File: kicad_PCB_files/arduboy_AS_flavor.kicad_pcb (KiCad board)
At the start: 2 copper layers, 50.6 x 82.6 mm, 119 parts, among them J1 SSD1306_SSH1106, J2 Expansion_port_NEW, J3 USB_B_Micro, Q1 2N7002, Q2 Si2301CDS, SW1 RST Button, SW2 UP Button, SW3 DOWN Button, SW4 LEFT Button, SW5 RIGHT Button, SW6 A Button, SW7 B Button, U1 ATmega32U4-MU, U1B1 ATmega32U4-AU, U2 W25Q128JVSIQ, U3 XC6206P33, U4 TP4054, U5 MPU-6050, Y1 16MHz

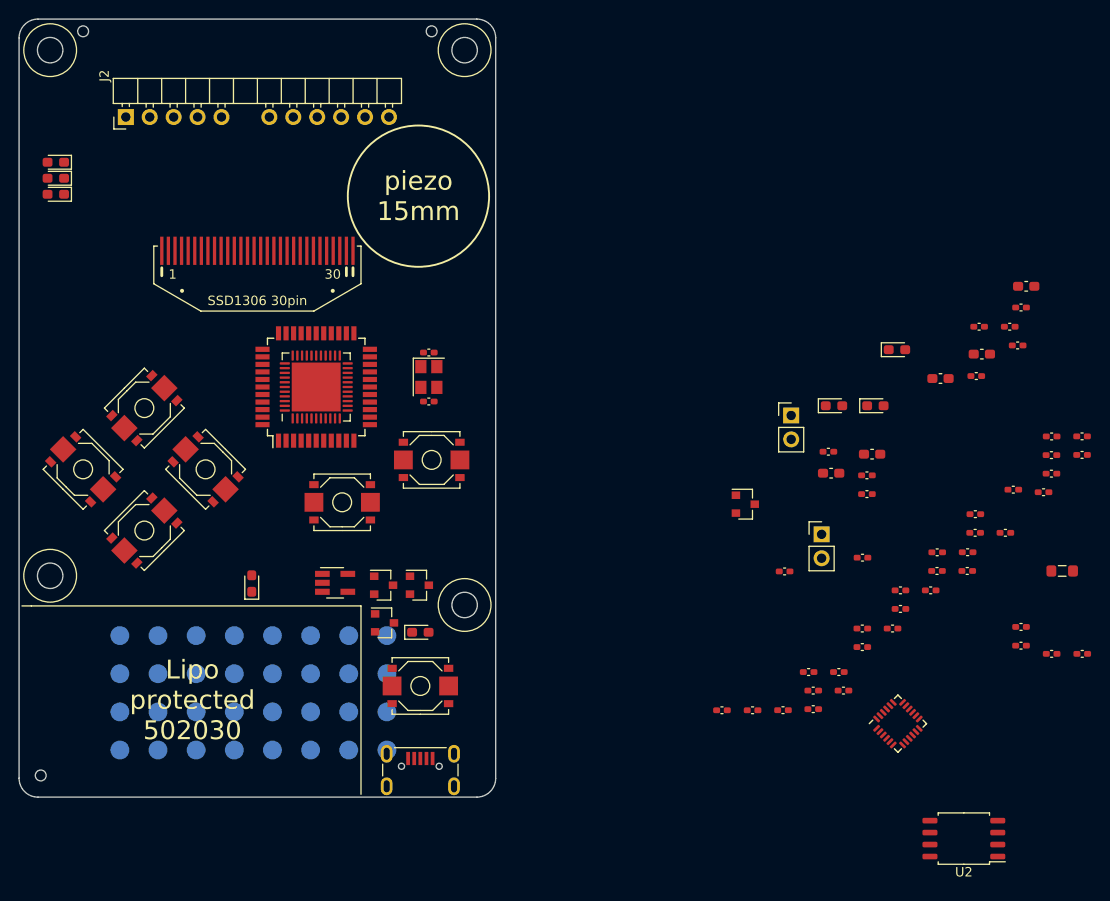
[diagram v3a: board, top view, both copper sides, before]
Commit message: Changed reset circuit Continued PCB placement feasibility Changed piezo footprint
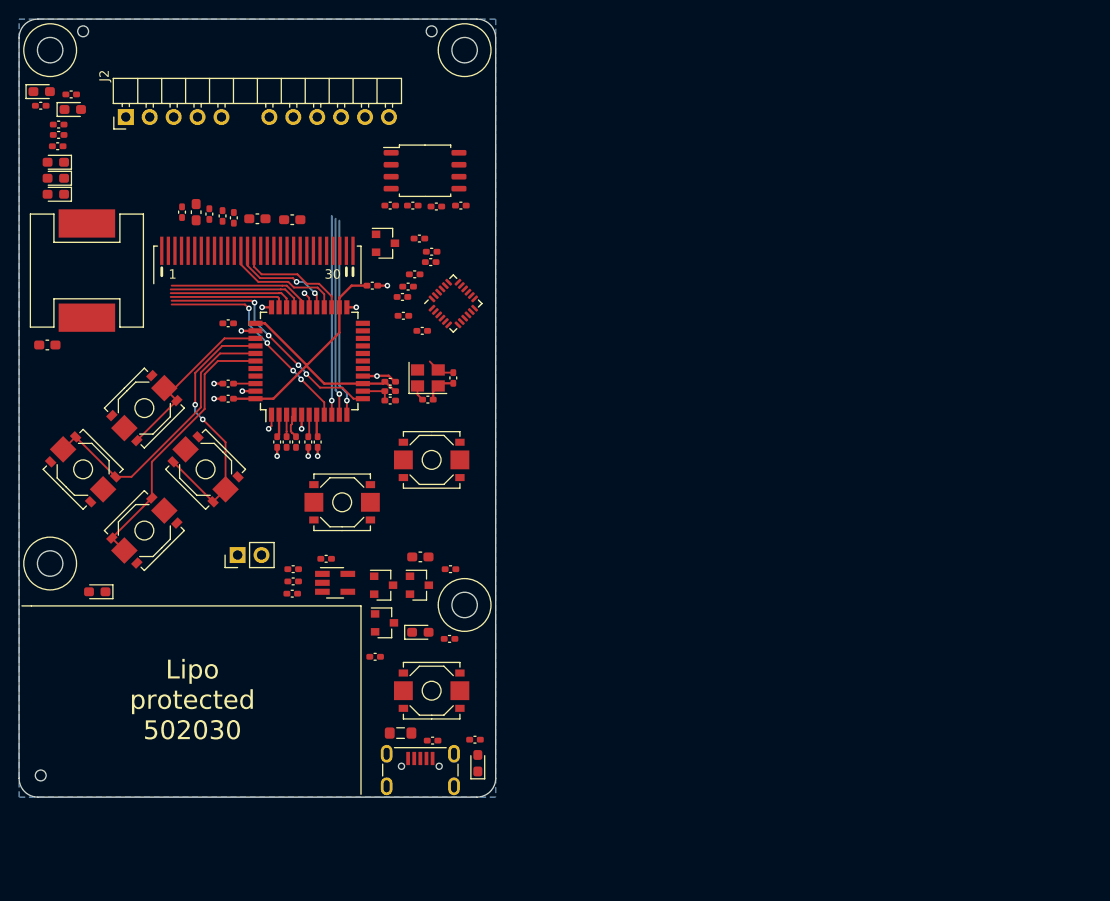
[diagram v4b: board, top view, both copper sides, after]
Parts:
- removed TP1: GYRO_INT, TestPoint:TestPoint_Pad_D2.0mm
- removed TP10: D4/D4/~OLED_DC, TestPoint:TestPoint_Pad_D2.0mm
- removed TP11: D14/PB3/MISO, TestPoint:TestPoint_Pad_D2.0mm
- removed TP12: D6/D7/~OLED_RST, TestPoint:TestPoint_Pad_D2.0mm
- removed TP13: D16/PB2/MOSI, TestPoint:TestPoint_Pad_D2.0mm
- removed TP14: D12/D6/~OLED_CS, TestPoint:TestPoint_Pad_D2.0mm
- removed TP15: D15/PB1/SCK, TestPoint:TestPoint_Pad_D2.0mm
- removed TP16: USB_ID, TestPoint:TestPoint_Pad_D2.0mm
- removed TP17: D7/E6/A, TestPoint:TestPoint_Pad_D2.0mm
- removed TP18: A4/F1/EN, TestPoint:TestPoint_Pad_D2.0mm
- removed TP19: D8/PB4/B, TestPoint:TestPoint_Pad_D2.0mm
- removed TP2: D2/PD1/SDA+FLASH_CS, TestPoint:TestPoint_Pad_D2.0mm
- removed TP20: A5/F0, TestPoint:TestPoint_Pad_D2.0mm
- removed TP21: A0/PF7/UP, TestPoint:TestPoint_Pad_D2.0mm
- removed TP22: D1/PD3/TX, TestPoint:TestPoint_Pad_D2.0mm
- removed TP23: A1/F6/RIGHT, TestPoint:TestPoint_Pad_D2.0mm
- removed TP24: D0/PD2/RX, TestPoint:TestPoint_Pad_D2.0mm
- removed TP25: A2/F5/LEFT, TestPoint:TestPoint_Pad_D2.0mm
- removed TP26: D13/PC7/SPKR2, TestPoint:TestPoint_Pad_D2.0mm
- removed TP27: A3/F4/DOWN, TestPoint:TestPoint_Pad_D2.0mm
- removed TP28: D5/PC6/SPKR1, TestPoint:TestPoint_Pad_D2.0mm
- removed TP29: 3V3, TestPoint:TestPoint_Pad_D2.0mm
- removed TP3: ~RST, TestPoint:TestPoint_Pad_D2.0mm
- removed TP30: VCC, TestPoint:TestPoint_Pad_D2.0mm
- removed TP31: 5V_USB, TestPoint:TestPoint_Pad_D2.0mm
- removed TP32: GND, TestPoint:TestPoint_Pad_D2.0mm
- removed TP4: D3/PD0/SCL, TestPoint:TestPoint_Pad_D2.0mm
- removed TP5: D11/PB7/~LED_G, TestPoint:TestPoint_Pad_D2.0mm
- removed TP6: D17/PB0/~RX_LED, TestPoint:TestPoint_Pad_D2.0mm
- removed TP7: D10/PB6/~LED_R, TestPoint:TestPoint_Pad_D2.0mm
- removed TP8: D30/D5/~TX_LED, TestPoint:TestPoint_Pad_D2.0mm
- removed TP9: D9/PB5/~LED_B, TestPoint:TestPoint_Pad_D2.0mm
- removed the U1 at (53.2, 60.8)
- JP1: footprint Connector_PinHeader_2.54mm:PinHeader_1x02_P2.54mm_Vertical -> arduboy:CPT-12123-81-SMT
- moved R13 112.9 mm to (24.0, 30.9)
- moved R10 104.5 mm to (25.9, 32.9)
- moved R15 104.1 mm to (24.7, 56.3)
- moved R14 104.0 mm to (27.2, 29.7)
- moved R11 95.7 mm to (25.9, 34.0)
- moved C5 93.8 mm to (39.0, 42.2), turned to 90 degrees
- moved R9 93.5 mm to (25.8, 35.2)
- moved C6 93.4 mm to (41.9, 42.4), turned to 90 degrees
- moved D9 91.1 mm to (27.4, 31.3)
- moved U2 91.1 mm to (64.8, 37.8), turned to 0 degrees
- moved C11 91.0 mm to (44.5, 42.8), turned to 90 degrees
- moved D8 90.5 mm to (24.1, 29.4)
- moved C13 81.9 mm to (50.7, 82.7)
- moved C10 81.7 mm to (43.3, 42.6), turned to 90 degrees
- moved R17 81.0 mm to (40.5, 42.2), turned to 90 degrees
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- renumbered U1B1 to U1
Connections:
- C17 pad 1: VBUS -> +5V
- C18 pad 1: VBUS -> +5V
- C2 pad 1: XTAL2 -> XTAL1
- C3 pad 1: XTAL1 -> XTAL2
- Y1 pad 1: XTAL1 -> XTAL2
- Y1 pad 3: XTAL2 -> XTAL1
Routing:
- net VCC: track 0.00 -> 39.4 mm
- net Btn_LEFT: track 0.00 -> 30.3 mm
- net Btn_DOWN: track 0.00 -> 29.3 mm
- net Btn_RIGHT: track 0.00 -> 29.2 mm, vias 0 -> 2
- net LED_G: track 0.00 -> 25.8 mm, vias 0 -> 4
- net RX_LED: track 0.00 -> 23.0 mm, vias 0 -> 4
- net SCK: track 0.00 -> 21.1 mm, vias 0 -> 1
- net MOSI: track 0.00 -> 21.0 mm, vias 0 -> 1
- net MISO: track 0.00 -> 20.9 mm, vias 0 -> 1
- net Btn_UP: track 0.00 -> 19.7 mm
- net GND: track 0.00 -> 19.2 mm, vias 0 -> 12
- net LED_B: track 0.00 -> 15.2 mm
- net LED_R: track 0.00 -> 14.4 mm
- net SPKR1: track 0.00 -> 13.5 mm
- net OLED_CS: track 0.00 -> 13.0 mm
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- added copper zone on B.Cu, net GND
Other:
- net class Default: trace_width 0.25 -> 0.2; via_dia 0.8 -> 0.6; via_drill 0.4 -> 0.3
- net class Power added: clearance 0.2, trace_width 0.25, via_dia 0.6, via_drill 0.3
- rule pad_to_mask_clearance: 0 -> 0.05
- rule trace_min: 0.2 -> 0.15
- board text removed: "Todo: Add dpad hole"
- board text removed: "piezo 15mm"

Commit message: Major changes, practically v2
Changed board shape
Changed a great part of the schematic
Component placement done
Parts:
- removed C23: 10nF, no_refdes:0402_HandSolder
- removed C24, C26: 100nF, no_refdes:0402_HandSolder
- removed C25: 2.2nF, no_refdes:0402_HandSolder
- removed C27: 1uF, no_refdes:0402_HandSolder
- removed D1: BAV70, Package_TO_SOT_SMD:SOT-23
- removed D5, D6: Yellow, LED_SMD:LED_0603_1608Metric_Pad1.05x0.95mm_HandSolder
- removed JP1: Speaker, arduboy:CPT-12123-81-SMT
- removed JP2: LiPo, Connector_PinHeader_2.54mm:PinHeader_1x02_P2.54mm_Vertical
- removed Q1: 2N7002, Package_TO_SOT_SMD:SOT-23
- removed Q2: Si2301CDS, Package_TO_SOT_SMD:SOT-23
- removed R15: 220, no_refdes:0603_HandSolder
- removed U5: MPU-6050, Sensor_Motion:InvenSense_QFN-24_4x4mm_P0.5mm
- added BZ1: Buzzer, arduboy:Buzzer_KLJ-5020, F.Cu at (68.0, 51.0)
- added R22: 120, no_refdes:0402_HandSolder, F.Cu at (50.9, 34.0)
- added R23: 120, no_refdes:0402_HandSolder, F.Cu at (53.3, 34.0)
- added R24: 120, no_refdes:0402_HandSolder, F.Cu at (55.9, 34.0)
- added TP1: Lipo [+], TestPoint:TestPoint_Pad_2.0x2.0mm, F.Cu at (34.8, 88.0)
- added TP16: Lipo (-), TestPoint:TestPoint_Pad_D2.0mm, F.Cu at (48.0, 80.5)
- C1: value 100nF -> 10uF; footprint no_refdes:0402_HandSolder -> no_refdes:0603_HandSolder
- C15: value 2.2uF -> 4.7uF
- C8: value 1uF -> 10uF; footprint no_refdes:0402_HandSolder -> no_refdes:0603_HandSolder
- C9: value 1uF -> 4.7uF; footprint no_refdes:0402_HandSolder -> no_refdes:0603_HandSolder
- J1: value SSD1306_SSH1106 -> SSD1306
- J2: footprint arduboy:PinHeader_1x12_P2.54mm_SLOTTED_ROTATED -> arduboy:ExpansionPort_SMD
- R12: value 6.8k -> 1.2k
- R13: value 3.3k -> 1.2k
- R14: value 3.3k -> 4.7k
- R18, R19: value 4.7k -> 120
- R5, R8: value 10k -> 120
- R6: value 6.8k -> 120
- R7: value 3.3k -> 120
- SW1: value RST Button -> ON/OFF; footprint arduboy:button_TS-1187A-B-A-B -> arduboy:Switch_DPDT_MSK12CO2-BDM
- U3: value XC6206P33 -> SRV05-4; footprint Package_TO_SOT_SMD:SOT-23 -> Package_TO_SOT_SMD:SOT-23-6
- moved H5 87.1 mm to (25.5, 100.5)
- moved R6 72.9 mm to (35.6, 34.0), turned to 180 degrees
- moved R5 61.4 mm to (33.0, 34.0), turned to 180 degrees
- moved R7 61.0 mm to (38.1, 34.0), turned to 180 degrees
- moved D7 60.4 mm to (68.5, 36.0), turned to 0 degrees
- moved U3 54.1 mm to (38.2, 94.8), turned to -90 degrees
- moved H7 54.0 mm to (25.5, 25.5)
- moved R8 53.3 mm to (40.6, 34.0), turned to 180 degrees
- moved D8 45.1 mm to (68.5, 37.5)
- moved C7 44.9 mm to (44.0, 38.8), turned to 90 degrees
- moved R12 44.3 mm to (63.0, 37.5), turned to 180 degrees
- moved H4 43.5 mm to (68.5, 25.5)
- moved D9 41.8 mm to (68.5, 39.0)
- moved R3 41.5 mm to (24.7, 45.6), turned to 180 degrees
- moved U2 41.0 mm to (26.0, 51.0), turned to -90 degrees
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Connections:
- net /~HOLD renamed /~{HOLD}
- net /~WP renamed /~{WP}
- net Net-(R16-Pad1) renamed /PROG
- C1 pad 1: RST -> VCC
- C1 pad 2: Net-(C1-Pad2) -> GND
- C9 pad 1: +3V3 -> SPKR1
- C9 pad 2: GND -> Net-(BZ1-Pad1)
- D7 pad 2: Net-(D7-Pad2) -> +5V
- D8 pad 1: GND -> Net-(D8-Pad1)
- D8 pad 2: Net-(D8-Pad2) -> VCC
- D9 pad 1: GND -> Net-(D9-Pad1)
- D9 pad 2: Net-(D9-Pad2) -> VCC
- J1 pad 1: Net-(J1-Pad1) -> unconnected-(J1-Pad1)
- J1 pad 20: Net-(J1-Pad20) -> unconnected-(J1-Pad20)
- J1 pad 21: Net-(J1-Pad21) -> unconnected-(J1-Pad21)
- J1 pad 22: Net-(J1-Pad22) -> unconnected-(J1-Pad22)
- J1 pad 23: Net-(J1-Pad23) -> unconnected-(J1-Pad23)
- J1 pad 24: Net-(J1-Pad24) -> unconnected-(J1-Pad24)
- J1 pad 25: Net-(J1-Pad25) -> unconnected-(J1-Pad25)
- J1 pad 29: Net-(J1-Pad29) -> unconnected-(J1-Pad29)
- J1 pad 30: Net-(J1-Pad30) -> unconnected-(J1-Pad30)
- J2 pad 10: SCL_3V3 -> Net-(J2-Pad10)
- J2 pad 11: SDA+FCS -> Net-(J2-Pad11)
- J2 pad 12: TX -> Net-(J2-Pad12)
- J2 pad 3: RST -> Net-(J2-Pad3)
- J2 pad 4: SCLK -> Net-(J2-Pad4)
- J2 pad 5: MOSI -> Net-(J2-Pad5)
- J2 pad 6: MISO -> Net-(J2-Pad6)
- J2 pad 8: A5 -> Net-(J2-Pad8)
- J2 pad 9: RX -> Net-(J2-Pad9)
- J3 pad 4: Net-(J3-Pad4) -> unconnected-(J3-Pad4)
- J3 pad 6: Net-(J3-Pad6) -> unconnected-(J3-Pad6)
- R12 pad 1: +5V -> Net-(D8-Pad1)
- R12 pad 2: Net-(D7-Pad2) -> RX_LED
- R13 pad 1: RX_LED -> Net-(D9-Pad1)
- R13 pad 2: Net-(D8-Pad2) -> TX_LED
- R14 pad 1: TX_LED -> Net-(D7-Pad1)
- R14 pad 2: Net-(D9-Pad2) -> ~{CHRG}
- R18 pad 1: +3V3 -> A5
- R18 pad 2: SCL_3V3 -> Net-(J2-Pad8)
- R19 pad 1: +3V3 -> MISO
- R19 pad 2: SDA+FCS -> Net-(J2-Pad6)
- R5 pad 1: EN -> TX
- R5 pad 2: GND -> Net-(J2-Pad12)
- R6 pad 1: +5V -> SDA+FCS
- R6 pad 2: Net-(D5-Pad2) -> Net-(J2-Pad11)
- R7 pad 1: VCC -> SCL
- R7 pad 2: Net-(D6-Pad2) -> Net-(J2-Pad10)
- R8 pad 1: +BATT -> RX
- R8 pad 2: ~PWR_EN -> Net-(J2-Pad9)
- SW1 pad 1: GND -> VCC
- SW1 pad 2: Net-(D1-Pad3) -> +BATT
- U1 pad 18: SCL_3V3 -> SCL
- U1 pad 40: EN -> A4
- U3 pad 1: GND -> /USB_D+
- U3 pad 2: +3V3 -> GND
- U3 pad 3: VCC -> /USB_D-
- U4 pad 1: Net-(D7-Pad1) -> ~{CHRG}
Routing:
- net VCC: track 39.4 -> 0.00 mm
- net Btn_LEFT: track 30.3 -> 0.00 mm
- net Btn_DOWN: track 29.3 -> 0.00 mm
- net Btn_RIGHT: track 29.2 -> 0.00 mm, vias 2 -> 0
- net LED_G: track 25.8 -> 0.00 mm, vias 4 -> 0
- net RX_LED: track 23.0 -> 0.00 mm, vias 4 -> 0
- net SCK: track 21.1 -> 0.00 mm, vias 1 -> 0
- net MOSI: track 21.0 -> 0.00 mm, vias 1 -> 0
- net MISO: track 20.9 -> 0.00 mm, vias 1 -> 0
- net Btn_UP: track 19.7 -> 0.00 mm
- net GND: track 19.2 -> 0.00 mm, vias 12 -> 0
- net LED_B: track 15.2 -> 0.00 mm
- net LED_R: track 14.4 -> 0.00 mm
- net SPKR1: track 13.5 -> 0.00 mm
- net OLED_CS: track 13.0 -> 0.00 mm
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- added copper zone on In1.Cu, net GND
- removed copper zone on B.Cu, net GND
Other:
- board size 50.6 x 82.6 mm -> 50 x 82 mm
- copper layers 2 -> 4
- net class Default removed
- net class Power removed
- board text added: "JLCJLCJLCJLC"
